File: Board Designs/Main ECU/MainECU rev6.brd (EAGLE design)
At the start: 120.6 x 78.9 mm, 177 parts, among them J1 JUMPER, J2 JUMPER, J3 JUMPER, J4 JUMPER, Q12 P-CHANNEL_MOSFET_DMP3099L-7, X1 CONNECTOR-37, X2 CONNECTOR-4AUTOSPORT, X3 CONNECTOR-4NANO-FIT-VERTICAL-4, X4 CONNECTOR-4NANO-FIT-VERTICAL-4

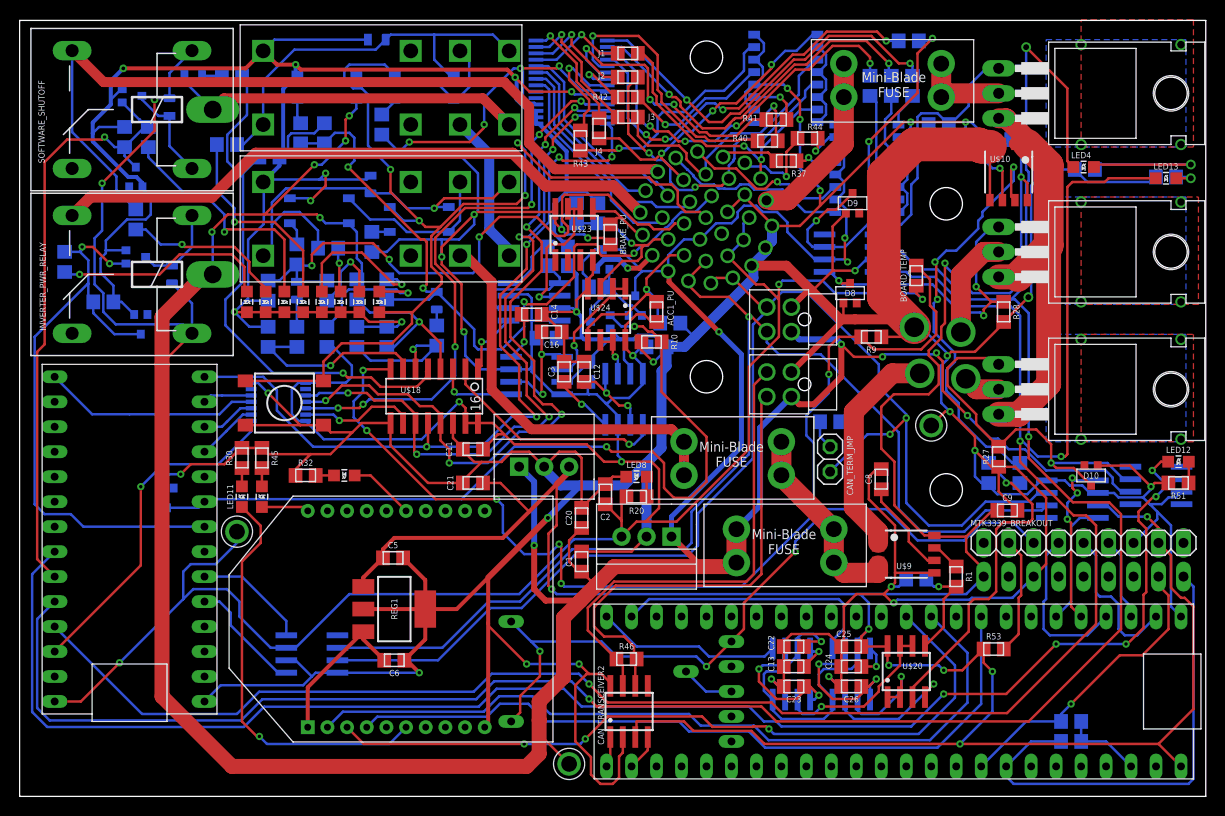
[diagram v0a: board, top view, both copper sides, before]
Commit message: Main ECU rev6: Implement latching without solid state relays, Fix swapped p-mosfet circuit pins, Move 5V test point to more accessible location, Change DPDT relays to TE RT424009
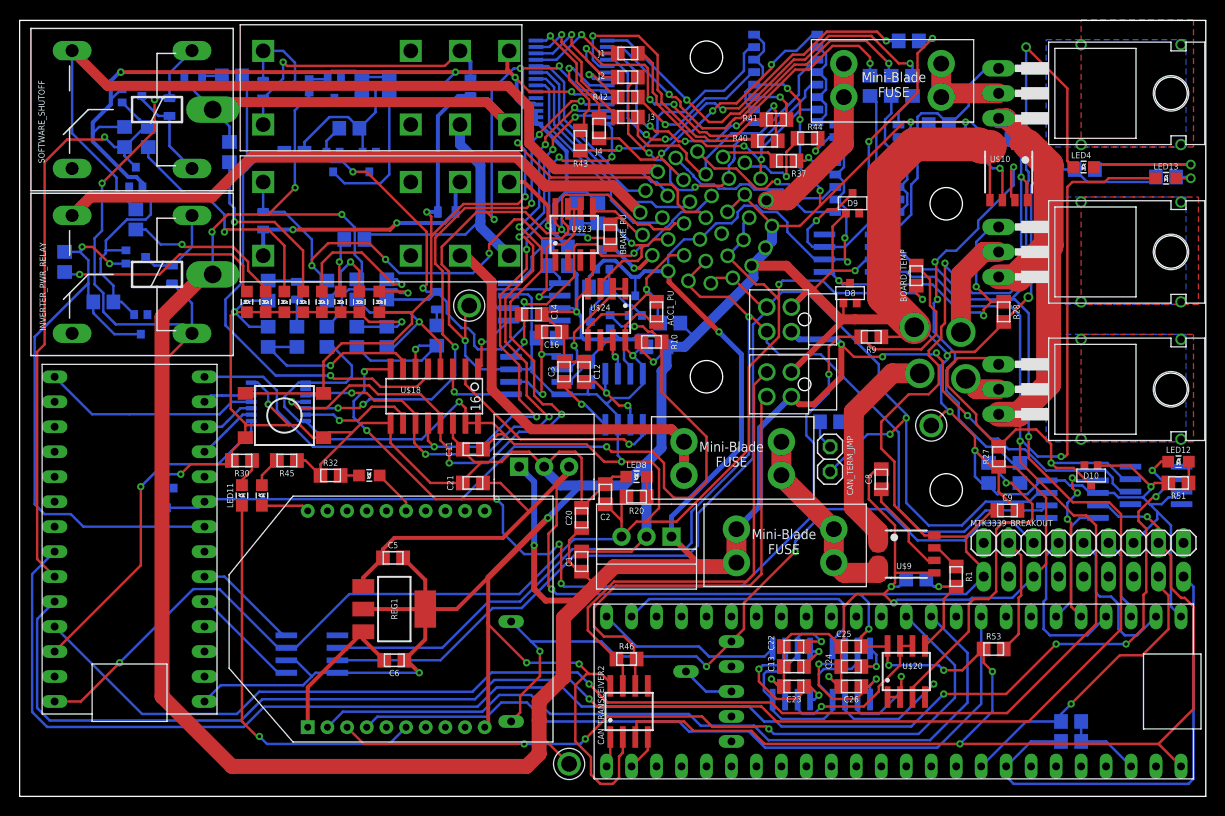
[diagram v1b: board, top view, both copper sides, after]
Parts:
- removed BMS_LATCH_SSR, BMS_SSR, IMD_LATCH_SSR, IMD_SSR: CPC1002N, HyTechDevices:SOP04
- removed R11: 510, HyTechDevices:0805
- removed R21: 3.3k, HyTechDevices:0805
- added D15, D16: TS4148 RYG, HyTechDevices:0805_D
- added D17, D18: MMBZ5246BLT1G, HyTechDevices:SOT23
- added Q1: P-CHANNEL_MOSFET_DMP3099L-7, HyTechDevices:SOT23
- added Q2: (no value), HyTechDevices:SOT23
- D1, D2, D3, D4, D5, D6, D7: value DIODE0805 -> TS4148 RYG
- IMD_SHUTDOWN, IMD_SHUTDOWN1: value G2RL-2-DC12 -> RT424009; device HyTechDevices:G2RL-2 -> HyTechDevices:RELAY_DPDT
- R12: value 1k -> 10k
- R18: value 2.2k -> 2k
- moved U$11 33.0 mm to (45.7, 49.9)
- moved R12 15.8 mm to (34.8, 72.1), turned to 90 degrees
- moved D5 12.6 mm to (24.8, 71.9), turned to 90 degrees
- moved D6 11.5 mm to (24.8, 58.5), turned to 90 degrees
- moved R13 3.89 mm to (37.6, 72.1)
- moved R14 2.81 mm to (34.0, 56.6), turned to 0 degrees
- moved R19 2.59 mm to (33.5, 67.9), turned to 180 degrees
- moved R22 2.57 mm to (27.9, 65.4)
- moved R45 2.55 mm to (27.2, 34.2), turned to 180 degrees
- moved R32 2.54 mm to (31.6, 32.6)
- moved LED10 2.54 mm to (35.6, 32.6)
- moved S1 1.27 mm to (26.9, 38.7)
- moved R17 0.80 mm to (21.3, 65.5), turned to 270 degrees
- moved R30 0.25 mm to (22.6, 34.2), turned to 0 degrees
- moved LED11 0.13 mm to (22.6, 30.6)
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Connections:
- removed net BMS_COIL_PWR: BMS_LATCH_SSR.3, D5.C, IMD_SHUTDOWN1.4, IMD_SHUTDOWN1.COIL-, R17.1
- removed net IMD_COIL_PWR: D6.C, IMD_LATCH_SSR.3, IMD_SHUTDOWN.4, IMD_SHUTDOWN.COIL-, R14.1
- removed net N$18: BMS_SSR.1, R11.1
- removed net N$31: IMD_SSR.1, R21.2
- removed net N$5: IMD_LATCH_SSR.1, R12.1
- new net BMS_OK_SW: D5.C, IMD_SHUTDOWN1.COIL+, Q1.3
- new net N$16: Q2.3, R13.1
- net +12V: now also D17.3, Q1.2, Q12.2, R12.1; no longer BMS_SSR.4, IMD_SSR.4, Q12.3
- net +5V: no longer R12.2, R13.1
- net BMS_OK: now also D18.3, Q2.1; no longer R11.2
- net BMS_PWR_STEP: now also D16.A, D5.A, IMD_SHUTDOWN1.COIL-; no longer BMS_LATCH_SSR.4, BMS_SSR.3
- net BRAKE_LIGHT: now also Q12.3; no longer Q12.2
- net GND: now also D18.1, IMD_SHUTDOWN.4, IMD_SHUTDOWN1.4, Q2.2; no longer BMS_SSR.2, D5.A, D6.A, IMD_SHUTDOWN.COIL+, IMD_SHUTDOWN1.COIL+, IMD_SSR.2
- net IMD_PWR_STEP: now also D15.A, D6.A, IMD_SHUTDOWN.COIL-; no longer IMD_LATCH_SSR.4, IMD_SSR.3
- net LATCH_EXT_BUTTON: now also D15.C, D16.C; no longer BMS_LATCH_SSR.2, IMD_LATCH_SSR.2
- net N$12: now also D17.1, Q1.1, R12.2; no longer BMS_LATCH_SSR.1
- net OKHS: now also D6.C, IMD_SHUTDOWN.COIL+; no longer R21.1
- net SHUTDOWN_B: now also R14.1
- net SHUTDOWN_C: now also R17.1
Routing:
- net IMD_COIL_PWR: track 41.8 -> 0.00 mm, vias 1 -> 0
- net BMS_COIL_PWR: track 40.7 -> 0.00 mm
- net +5V: track 371.3 -> 336.0 mm, vias 15 -> 12
- net GND: track 921.4 -> 900.5 mm, vias 32 -> 31
- net N$16: track 0.00 -> 14.4 mm
- net SHUTDOWN_B: track 15.4 -> 28.3 mm
- net LATCH_EXT_BUTTON: track 105.4 -> 92.7 mm, vias 4 -> 3
- net BMS_PWR_STEP: track 17.1 -> 29.2 mm, vias 0 -> 1
- net BMS_OK_SW: track 0.00 -> 9.35 mm
- net IMD_PWR_STEP: track 17.1 -> 26.2 mm, vias 0 -> 2
- net OKHS: track 62.4 -> 70.8 mm
- net N$12: track 2.06 -> 8.96 mm
- net SCK_5V: track 75.7 -> 79.7 mm
- net SHUTDOWN_C: track 36.4 -> 40.0 mm
- net N$18: track 2.48 -> 0.00 mm
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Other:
- board text added: "Shutdown B"
- board text added: "Shutdown C"
- board text added: "Shutdown D"
- board text removed: "BMS Coil"
- board text removed: "IMD Coil"
- board text removed: "Shutdown"

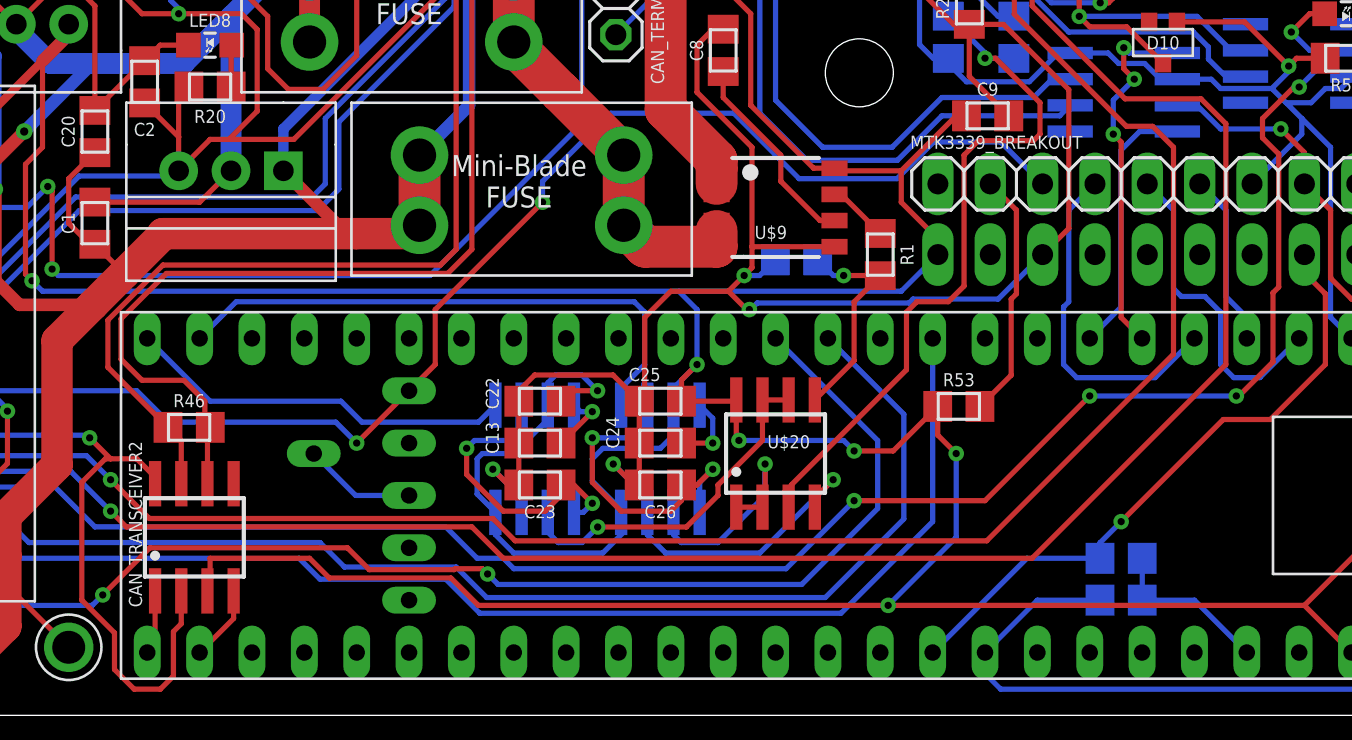
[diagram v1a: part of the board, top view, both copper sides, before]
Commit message: Main ECU rev5/6: Add jumpers to bypass MAX7480 current sensor filter circuits
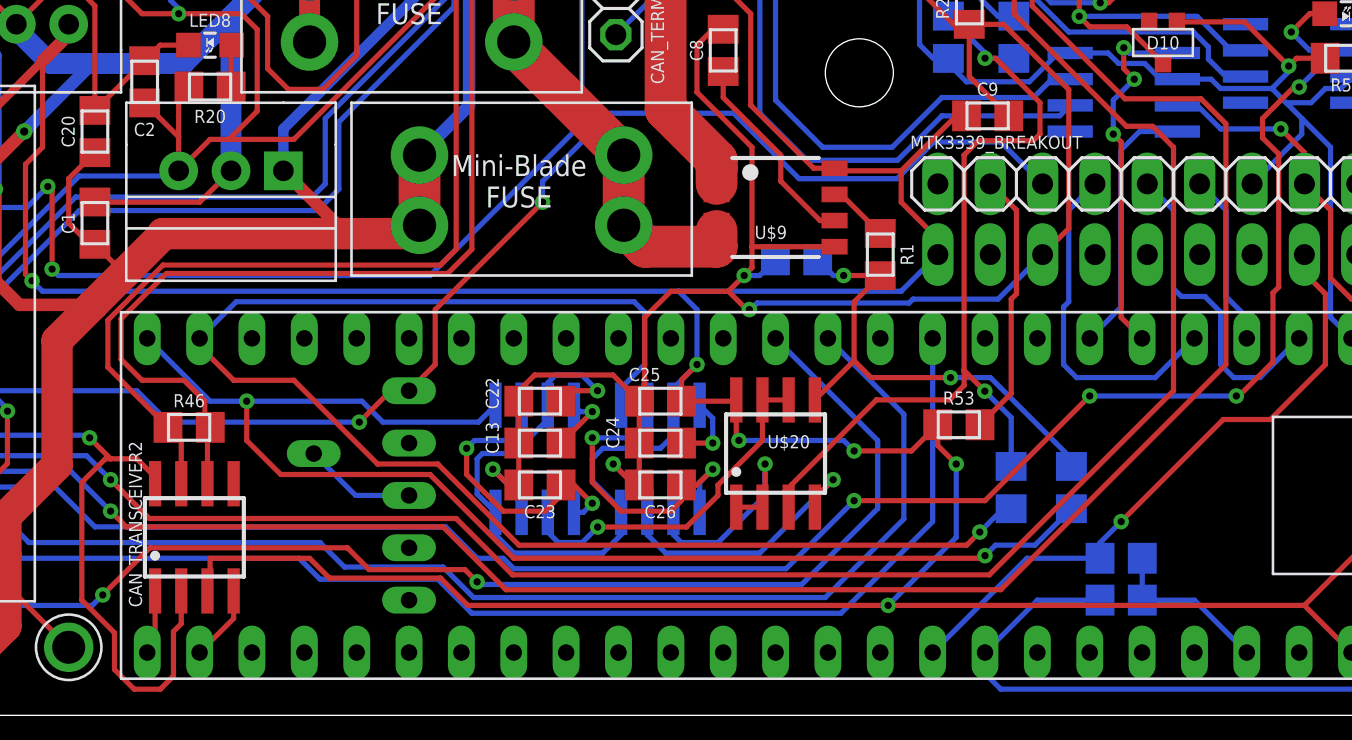
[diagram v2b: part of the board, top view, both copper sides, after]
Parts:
- added J5, J6: JUMPER, HyTechDevices:0805
- moved R53 0.89 mm to (99.1, 14.1)
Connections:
- net COOLINGSENSE: now also J5.2
- net COOLINGSENSE_FILT: now also J5.1
- net ECUSENSE: now also J6.2
- net ECUSENSE_FILT: now also J6.1
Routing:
- net ECUSENSE_FILT: track 18.9 -> 64.2 mm, vias 0 -> 2
- net COOLINGSENSE_FILT: track 27.5 -> 72.0 mm, vias 0 -> 1
- net ECUSENSE: track 10.7 -> 23.6 mm, vias 1 -> 2
- net COOLINGSENSE: track 34.9 -> 41.7 mm, vias 1 -> 2
- net FAN2CONTROL: track 210.7 -> 213.1 mm
- net FAN1CONTROL: track 226.9 -> 228.1 mm
- net TELEMETRY5V: track 322.4 -> 321.2 mm
- net N$7: track 12.1 -> 12.9 mm
- net VBAT_RTC: track 76.4 -> 75.6 mm

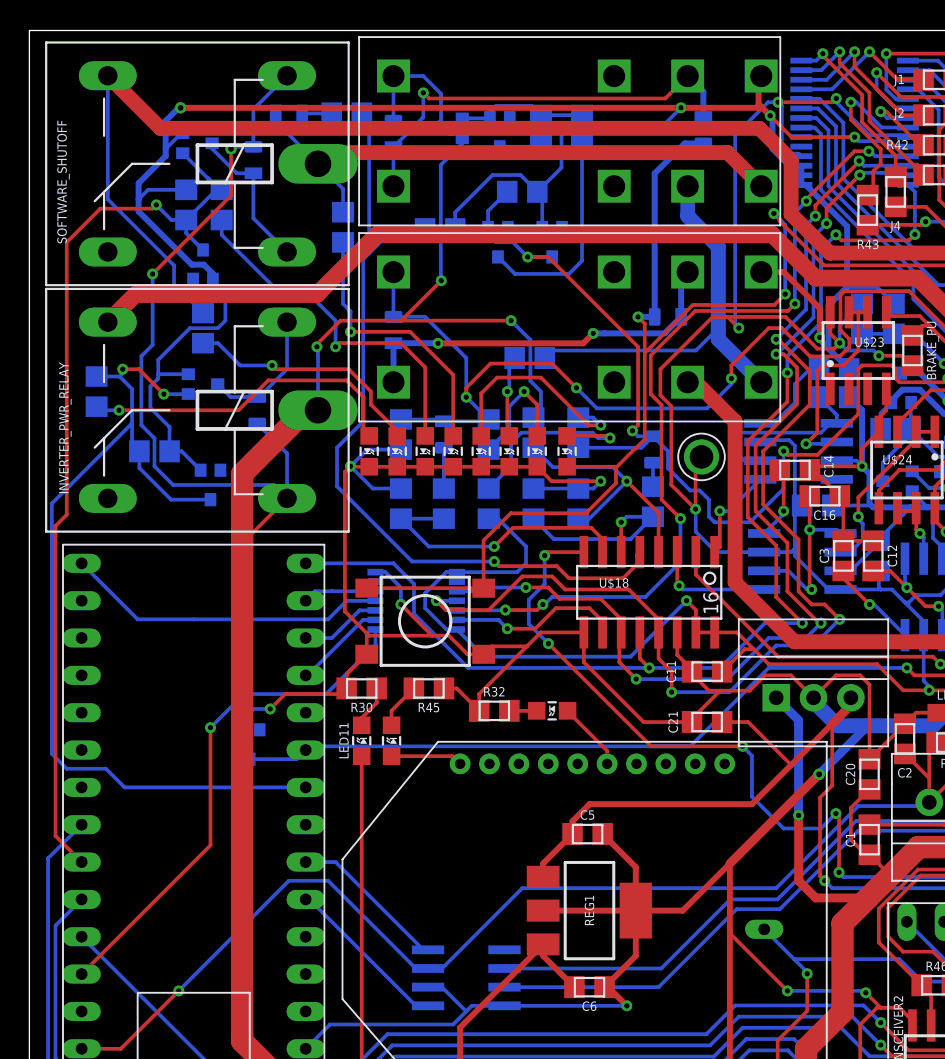
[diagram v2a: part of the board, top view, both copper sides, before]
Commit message: Main ECU rev5/6: Add voltage sensing for dashboard channels 11/12 and IMD/BMS shutdown circuit outputs
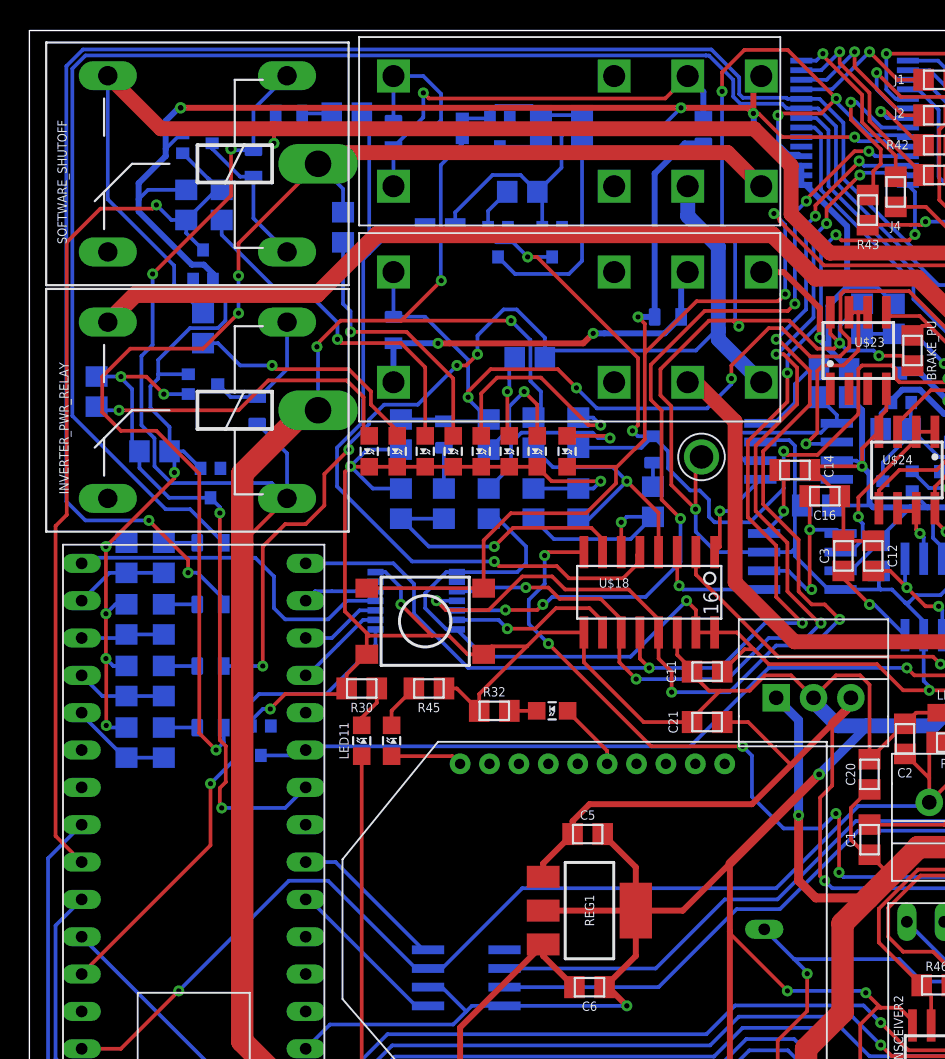
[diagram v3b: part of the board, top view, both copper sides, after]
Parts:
- added D19, D20, D21, D22: TS4148 RYG, HyTechDevices:0805_D
- added R11, R57, R59, R61: 43k, HyTechDevices:0805
- added R21, R58, R60, R62: 12k, HyTechDevices:0805
- moved D12 0.80 mm to (15.7, 30.6)
- moved D7 0.23 mm to (15.2, 69.9)
- moved D14 0.13 mm to (12.3, 48.1)
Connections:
- new net DASH_CTRL11_READ: R11.2, R21.1, U$1.A0
- new net DASH_CTRL12_READ: R57.2, R58.1, U$1.A1
- new net N$18: D19.C, R11.1
- new net N$31: D21.C, R59.1
- new net N$34: D22.C, R61.1
- new net N$5: D20.C, R57.1
- new net SHUTDOWN_B_READ: R59.2, R60.1, U$1.A2
- new net SHUTDOWN_C_READ: R61.2, R62.1, U$1.A3
- net DASH_CTRL11: now also D19.A
- net DASH_CTRL12: now also D20.A
- net GND: now also R21.2, R58.2, R60.2, R62.2
- net SHUTDOWN_B: now also D21.A
- net SHUTDOWN_C: now also D22.A; no longer D3.A
- net SHUTDOWN_D: now also D3.A
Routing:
- net DASH_CTRL12: track 21.2 -> 117.7 mm, vias 0 -> 2
- net DASH_CTRL11: track 18.4 -> 108.0 mm
- net SHUTDOWN_C: track 40.0 -> 90.6 mm, vias 0 -> 3
- net SHUTDOWN_B: track 28.3 -> 69.5 mm, vias 0 -> 4
- net GND: track 900.5 -> 927.5 mm, vias 31 -> 36
- net INVERTER_CTRL: track 62.8 -> 47.2 mm, vias 2 -> 4
- net +5V: track 336.0 -> 345.2 mm, vias 12 -> 13
- net SHUTDOWN_C_READ: track 0.00 -> 6.93 mm
- net DASH_CTRL11_READ: track 0.00 -> 6.37 mm
- net SHUTDOWN_B_READ: track 0.00 -> 6.17 mm
- net DASH_CTRL12_READ: track 0.00 -> 5.69 mm
- net SHUTDOWN_D: track 85.6 -> 88.5 mm, vias 0 -> 1
- net N$5: track 0.00 -> 2.28 mm
- net N$34: track 0.00 -> 2.28 mm
- net N$31: track 0.00 -> 2.28 mm
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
